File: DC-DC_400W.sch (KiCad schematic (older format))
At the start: 13 parts, among them J1 Conn_01x24, J10 Conn_01x05, J2 Conn_01x03, J3 Conn_01x05, J4 Conn_01x01, J5 Conn_01x01, J6 Conn_01x02, J7 Conn_01x01, J8 Conn_01x01, J9 Conn_01x01

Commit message: final 1.0 version
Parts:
- removed J10, J3: Conn_01x05, Connectors_Phoenix:PhoenixContact_MSTBVA-G_05x5.00mm_Vertical, symbol Conn_01x05
- added J11, J12: Conn_01x06, Connectors_Phoenix:PhoenixContact_MSTBVA-G_06x5.00mm_Vertical, symbol Conn_01x06
- added R3: 402R, Resistors_SMD:R_0603, symbol R
- R2: value 680R -> 560R
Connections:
- wire segments 57 -> 61
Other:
- moved on the sheet: J6
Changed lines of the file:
@@
 $EndComp
 Wire Wire Line
-	5600 2150 6550 2150
+	5250 2150 6550 2150
 Wire Wire Line
 	5800 2450 6550 2450
 Wire Wire Line
-	5600 2550 6550 2550
+	5250 2550 6550 2550
 Wire Wire Line
 	6550 2650 6050 2650
@@
 	5600 2550 5600 2500
 $Comp
-L GND #PWR04
-U 1 1 5A3FEBAC
-P 5100 4700
-F 0 "#PWR04" H 5100 4450 50  0001 C CNN
-F 1 "GND" H 5100 4550 50  0000 C CNN
-F 2 "" H 5100 4700 50  0001 C CNN
-F 3 "" H 5100 4700 50  0001 C CNN
-	1    5100 4700
-	1    0    0    -1
-$EndComp
-Wire Wire Line
-	5100 4600 5000 4600
-Wire Wire Line
-	5100 4500 5000 4500
-Wire Wire Line
-	5100 4400 5000 4400
-Wire Wire Line
-	5000 4300 5100 4300
-Wire Wire Line
-	5000 4200 5100 4200
-$Comp
 L Conn_01x02 J6
 U 1 1 5A4F84EC
-P 4800 2400
-F 0 "J6" H 4800 2500 50  0000 C CNN
-F 1 "Conn_01x02" H 4800 2200 50  0000 C CNN
-F 2 "custom:XT60" H 4800 2400 50  0001 C CNN
-F 3 "" H 4800 2400 50  0001 C CNN
-	1    4800 2400
-	-1   0    0    1
-$EndComp
-$Comp
-L +12V #PWR05
+P 4000 2400
+F 0 "J6" H 4000 2500 50  0000 C CNN
+F 1 "Conn_01x02" H 4000 2200 50  0000 C CNN
+F 2 "custom:XT60" H 4000 2400 50  0001 C CNN
+F 3 "" H 4000 2400 50  0001 C CNN
+	1    4000 2400
+	-1   0    0    1
+$EndComp
+$Comp
+L +12V #PWR04
 U 1 1 5A4F85E8
-P 5100 2200
-F 0 "#PWR05" H 5100 2050 50  0001 C CNN
-F 1 "+12V" H 5100 2340 50  0000 C CNN
-F 2 "" H 5100 2200 50  0001 C CNN
-F 3 "" H 5100 2200 50  0001 C CNN
-	1    5100 2200
-	1    0    0    -1
-$EndComp
-$Comp
-L GND #PWR06
+P 4300 2200
+F 0 "#PWR04" H 4300 2050 50  0001 C CNN
+F 1 "+12V" H 4300 2340 50  0000 C CNN
+F 2 "" H 4300 2200 50  0001 C CNN
+F 3 "" H 4300 2200 50  0001 C CNN
+	1    4300 2200
+	1    0    0    -1
+$EndComp
+$Comp
+L GND #PWR05
 U 1 1 5A4F8A4D
-P 5100 2500
-F 0 "#PWR06" H 5100 2250 50  0001 C CNN
-F 1 "GND" H 5100 2350 50  0000 C CNN
-F 2 "" H 5100 2500 50  0001 C CNN
-F 3 "" H 5100 2500 50  0001 C CNN
-	1    5100 2500
-	1    0    0    -1
-$EndComp
-Wire Wire Line
-	5000 2300 5100 2300
-Wire Wire Line
-	5100 2300 5100 2200
-Wire Wire Line
-	5000 2400 5100 2400
-Wire Wire Line
-	5100 2400 5100 2500
+P 4300 2500
+F 0 "#PWR05" H 4300 2250 50  0001 C CNN
+F 1 "GND" H 4300 2350 50  0000 C CNN
+F 2 "" H 4300 2500 50  0001 C CNN
+F 3 "" H 4300 2500 50  0001 C CNN
+	1    4300 2500
+	1    0    0    -1
+$EndComp
+Wire Wire Line
+	4200 2300 4300 2300
+Wire Wire Line
+	4300 2300 4300 2200
+Wire Wire Line
+	4200 2400 4300 2400
+Wire Wire Line
+	4300 2400 4300 2500
 $Comp
 L Conn_01x03 J2
@@
 $EndComp
 $Comp
-L GND #PWR07
+L GND #PWR06
 U 1 1 5A58C603
 P 5100 1450
-F 0 "#PWR07" H 5100 1200 50  0001 C CNN
+F 0 "#PWR06" H 5100 1200 50  0001 C CNN
 F 1 "GND" H 5100 1300 50  0000 C CNN
 F 2 "" H 5100 1450 50  0001 C CNN
@@
 $EndComp
 $Comp
-L +12V #PWR08
+L +12V #PWR07
 U 1 1 5A58C626
 P 5100 1050
-F 0 "#PWR08" H 5100 900 50  0001 C CNN
+F 0 "#PWR07" H 5100 900 50  0001 C CNN
 F 1 "+12V" H 5100 1190 50  0000 C CNN
 F 2 "" H 5100 1050 50  0001 C CNN
@@
 P 5800 2750
 F 0 "R2" H 5700 2800 50  0000 C CNN
-F 1 "680R" H 5650 2700 50  0000 C CNN
+F 1 "560R" H 5650 2700 50  0000 C CNN
 F 2 "Resistors_SMD:R_0603" V 5730 2750 50  0001 C CNN
 F 3 "" H 5800 2750 50  0001 C CNN
@@
 $EndComp
 $Comp
-L GND #PWR09
+L GND #PWR08
 U 1 1 5A5A0040
 P 5800 3400
-F 0 "#PWR09" H 5800 3150 50  0001 C CNN
+F 0 "#PWR08" H 5800 3150 50  0001 C CNN
 F 1 "GND" H 5800 3250 50  0000 C CNN
 F 2 "" H 5800 3400 50  0001 C CNN
@@
 $EndComp
 $Comp
-L GND #PWR010
+L GND #PWR09
 U 1 1 5A5A623B
 P 5100 6600
-F 0 "#PWR010" H 5100 6350 50  0001 C CNN
+F 0 "#PWR09" H 5100 6350 50  0001 C CNN
 F 1 "GND" H 5100 6450 50  0000 C CNN
 F 2 "" H 5100 6600 50  0001 C CNN
@@
 Connection ~ 5100 5550
 $Comp
-L Conn_01x05 J10
-U 1 1 5A5C6ADB
-P 4800 3650
-F 0 "J10" H 4800 3950 50  0000 C CNN
-F 1 "Conn_01x05" H 4800 3350 50  0000 C CNN
-F 2 "Connectors_Phoenix:PhoenixContact_MSTBVA-G_05x5.00mm_Vertical" H 4800 3650 50  0001 C CNN
-F 3 "" H 4800 3650 50  0001 C CNN
-	1    4800 3650
-	-1   0    0    1
-$EndComp
-$Comp
-L +5V #PWR011
-U 1 1 5A5CBC89
-P 5100 3350
-F 0 "#PWR011" H 5100 3200 50  0001 C CNN
-F 1 "+5V" H 5100 3490 50  0000 C CNN
-F 2 "" H 5100 3350 50  0001 C CNN
-F 3 "" H 5100 3350 50  0001 C CNN
-	1    5100 3350
-	1    0    0    -1
-$EndComp
-Wire Wire Line
-	5100 3850 5000 3850
-Wire Wire Line
-	5100 3350 5100 3850
-Wire Wire Line
-	5000 3450 5100 3450
-Connection ~ 5100 3450
-Wire Wire Line
-	5000 3550 5100 3550
-Connection ~ 5100 3550
-Wire Wire Line
-	5000 3650 5100 3650
-Connection ~ 5100 3650
-Wire Wire Line
-	5000 3750 5100 3750
-Connection ~ 5100 3750
-$Comp
-L Conn_01x05 J3
-U 1 1 5A5CC2F8
-P 4800 4400
-F 0 "J3" H 4800 4700 50  0000 C CNN
-F 1 "Conn_01x05" H 4800 4100 50  0000 C CNN
-F 2 "Connectors_Phoenix:PhoenixContact_MSTBVA-G_05x5.00mm_Vertical" H 4800 4400 50  0001 C CNN
-F 3 "" H 4800 4400 50  0001 C CNN
-	1    4800 4400
-	-1   0    0    1
-$EndComp
-Wire Wire Line
-	5100 4200 5100 4700
-Connection ~ 5100 4600
-Connection ~ 5100 4500
-Connection ~ 5100 4400
-Connection ~ 5100 4300
-$Comp
 L Conn_01x01 J4
 U 1 1 5A5DC987
@@
 	5000 6450 5100 6450
 Connection ~ 5100 6450
+$Comp
+L R R3
+U 1 1 5A7EB192
+P 5250 2350
+F 0 "R3" H 5150 2400 50  0000 C CNN
+F 1 "402R" H 5100 2300 50  0000 C CNN
+F 2 "Resistors_SMD:R_0603" V 5180 2350 50  0001 C CNN
+F 3 "" H 5250 2350 50  0001 C CNN
+	1    5250 2350
+	1    0    0    -1
+$EndComp
+Wire Wire Line
+	5250 2200 5250 2150
+Connection ~ 5600 2150
+Wire Wire Line
+	5250 2500 5250 2550
+Connection ~ 5600 2550
+$Comp
+L Conn_01x06 J11
+U 1 1 5A7EB3AF
+P 3850 3750
+F 0 "J11" H 3850 4050 50  0000 C CNN
+F 1 "Conn_01x06" H 3850 3350 50  0000 C CNN
+F 2 "Connectors_Phoenix:PhoenixContact_MSTBVA-G_06x5.00mm_Vertical" H 3850 3750 50  0001 C CNN
+F 3 "" H 3850 3750 50  0001 C CNN
+	1    3850 3750
+	-1   0    0    1
+$EndComp
+$Comp
+L Conn_01x06 J12
+U 1 1 5A7EB42F
+P 3850 4650
+F 0 "J12" H 3850 4950 50  0000 C CNN
+F 1 "Conn_01x06" H 3850 4250 50  0000 C CNN
+F 2 "Connectors_Phoenix:PhoenixContact_MSTBVA-G_06x5.00mm_Vertical" H 3850 4650 50  0001 C CNN
+F 3 "" H 3850 4650 50  0001 C CNN
+	1    3850 4650
+	-1   0    0    1
+$EndComp
+$Comp
+L +5V #PWR010
+U 1 1 5A7EB553
+P 4200 3350
+F 0 "#PWR010" H 4200 3200 50  0001 C CNN
+F 1 "+5V" H 4200 3490 50  0000 C CNN
+F 2 "" H 4200 3350 50  0001 C CNN
+F 3 "" H 4200 3350 50  0001 C CNN
+	1    4200 3350
+	1    0    0    -1
+$EndComp
+Wire Wire Line
+	4050 3950 4200 3950
+Wire Wire Line
+	4200 3950 4200 3350
+Wire Wire Line
+	4050 3450 4200 3450
+Connection ~ 4200 3450
+Wire Wire Line
+	4050 3550 4200 3550
+Connection ~ 4200 3550
+Wire Wire Line
+	4050 3650 4200 3650
+Connection ~ 4200 3650
+Wire Wire Line
+	4050 3750 4200 3750
+Connection ~ 4200 3750
+Wire Wire Line
+	4050 3850 4200 3850
+Connection ~ 4200 3850
+$Comp
+L GND #PWR011
+U 1 1 5A7EB885
+P 4150 4950
+F 0 "#PWR011" H 4150 4700 50  0001 C CNN
+F 1 "GND" H 4150 4800 50  0000 C CNN
+F 2 "" H 4150 4950 50  0001 C CNN
+F 3 "" H 4150 4950 50  0001 C CNN
+	1    4150 4950
+	1    0    0    -1
+$EndComp
+Wire Wire Line
+	4050 4350 4150 4350
+Wire Wire Line
+	4150 4350 4150 4950
+Wire Wire Line
+	4050 4450 4150 4450
+Connection ~ 4150 4450
+Wire Wire Line
+	4050 4550 4150 4550
+Connection ~ 4150 4550
+Wire Wire Line
+	4050 4650 4150 4650
+Connection ~ 4150 4650
+Wire Wire Line
+	4050 4750 4150 4750
+Connection ~ 4150 4750
+Wire Wire Line
+	4050 4850 4150 4850
+Connection ~ 4150 4850
 $EndSCHEMATC

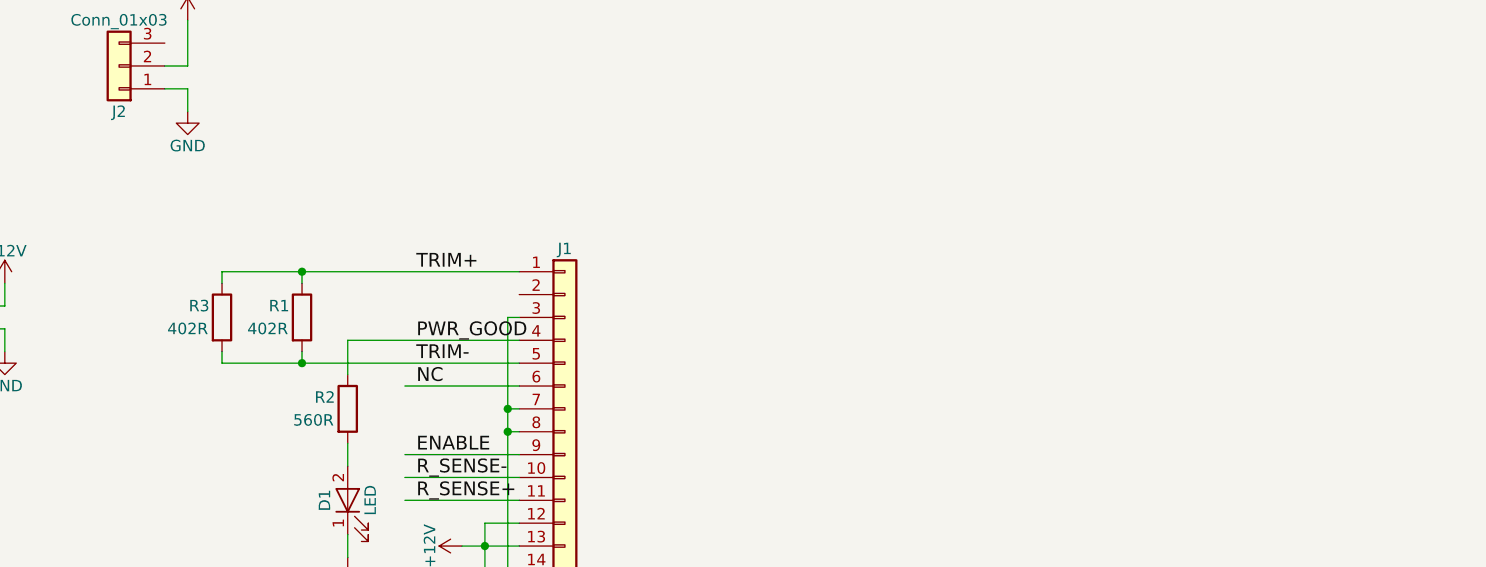
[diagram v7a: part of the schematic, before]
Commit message: correct R1 and R3 in schematic
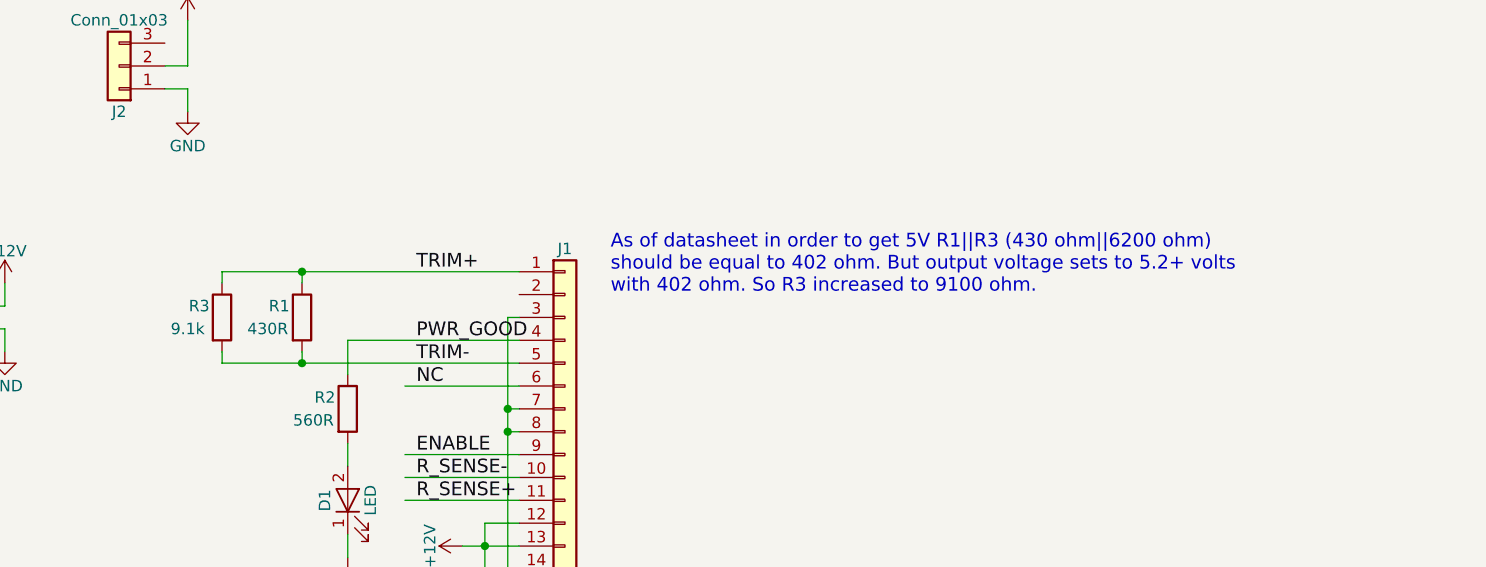
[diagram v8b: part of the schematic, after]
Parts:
- R1: value 402R -> 430R
- R3: value 402R -> 9.1k
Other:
- note added: "As of datasheet in order to get 5V R1||R3 (430 ohm||6200 ohm) \nshould be equal to 402 ohm. But output voltage sets to 5.2+ volts \nwith 402 ohm. So R3 increased to 9100 ohm."
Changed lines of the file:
@@
 P 5600 2350
 F 0 "R1" H 5500 2400 50  0000 C CNN
-F 1 "402R" H 5450 2300 50  0000 C CNN
+F 1 "430R" H 5450 2300 50  0000 C CNN
 F 2 "Resistors_SMD:R_0603" V 5530 2350 50  0001 C CNN
 F 3 "" H 5600 2350 50  0001 C CNN
@@
 P 5250 2350
 F 0 "R3" H 5150 2400 50  0000 C CNN
-F 1 "402R" H 5100 2300 50  0000 C CNN
+F 1 "9.1k" H 5100 2300 50  0000 C CNN
 F 2 "Resistors_SMD:R_0603" V 5180 2350 50  0001 C CNN
 F 3 "" H 5250 2350 50  0001 C CNN
@@
 	4050 4850 4150 4850
 Connection ~ 4150 4850
+Text Notes 6950 2250 0    60   ~ 0
+As of datasheet in order to get 5V R1||R3 (430 ohm||6200 ohm) \nshould be equal to 402 ohm. But output voltage sets to 5.2+ volts \nwith 402 ohm. So R3 increased to 9100 ohm.
 $EndSCHEMATC
